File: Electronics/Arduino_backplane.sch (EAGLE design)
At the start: 40 parts, among them IC1 4013N, IC2 MCP4802, IC3 MCP4802, Q1 BF199, Q5 BF199, X1 M25-HD-20, X2 M25-HD-20

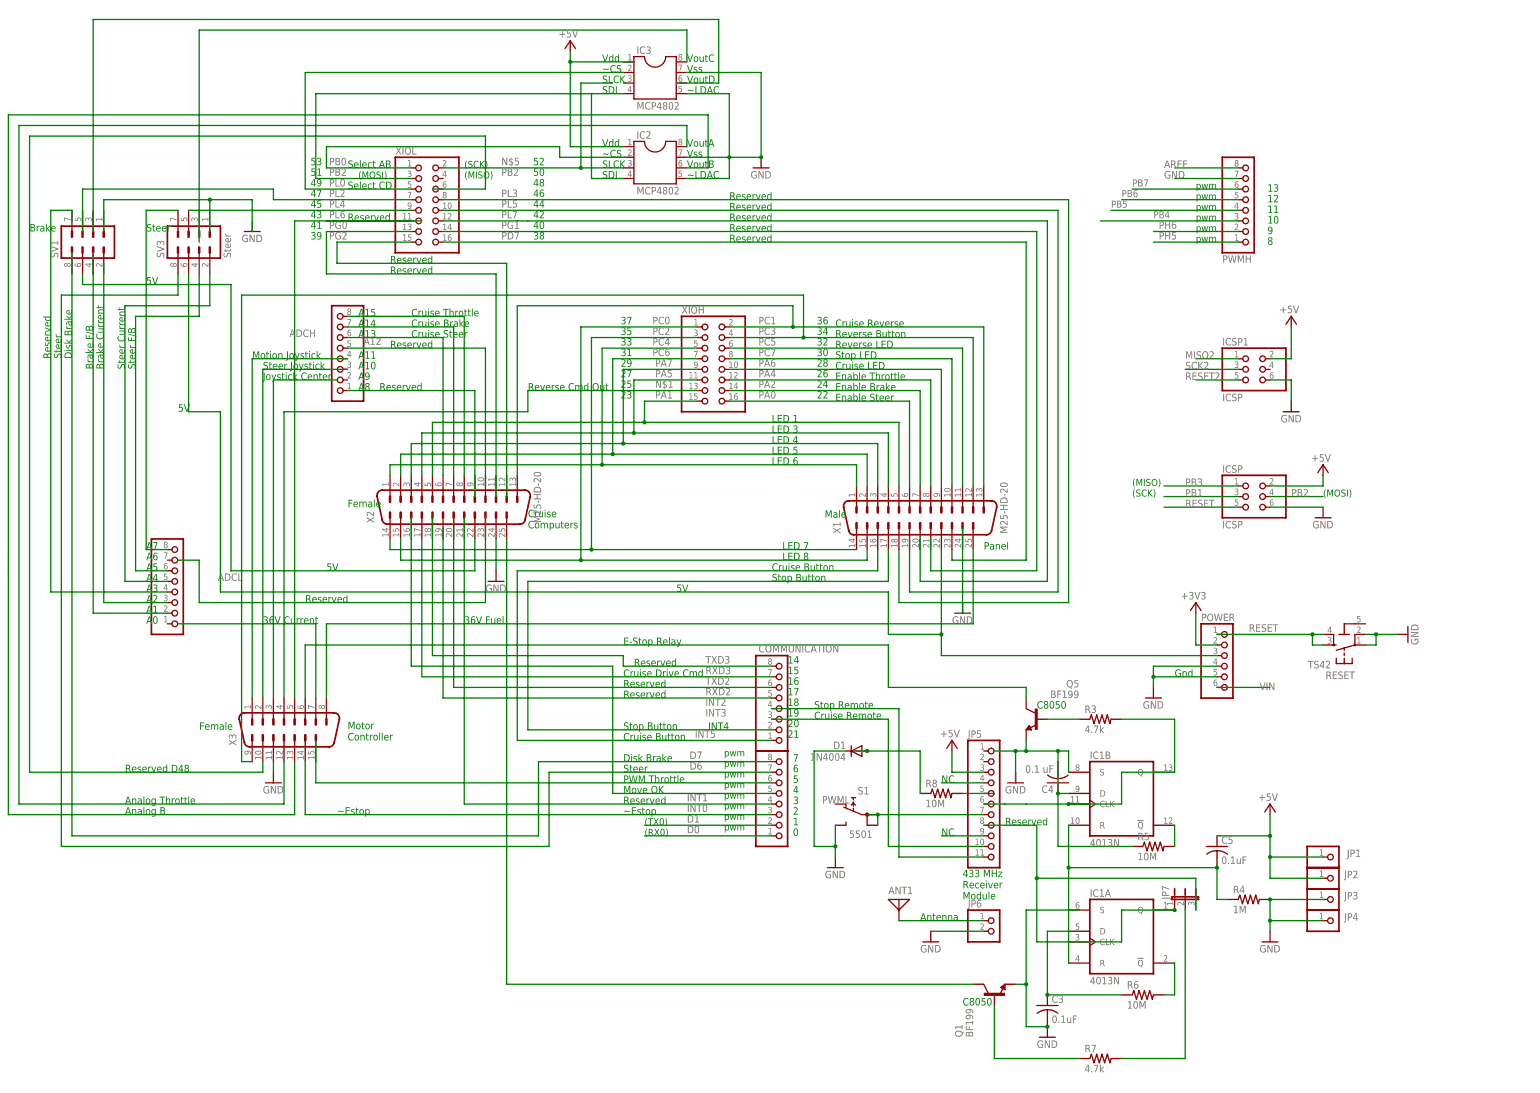
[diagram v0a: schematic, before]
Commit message: Board layout improved, closer to Arduino pins. Signals renamed.
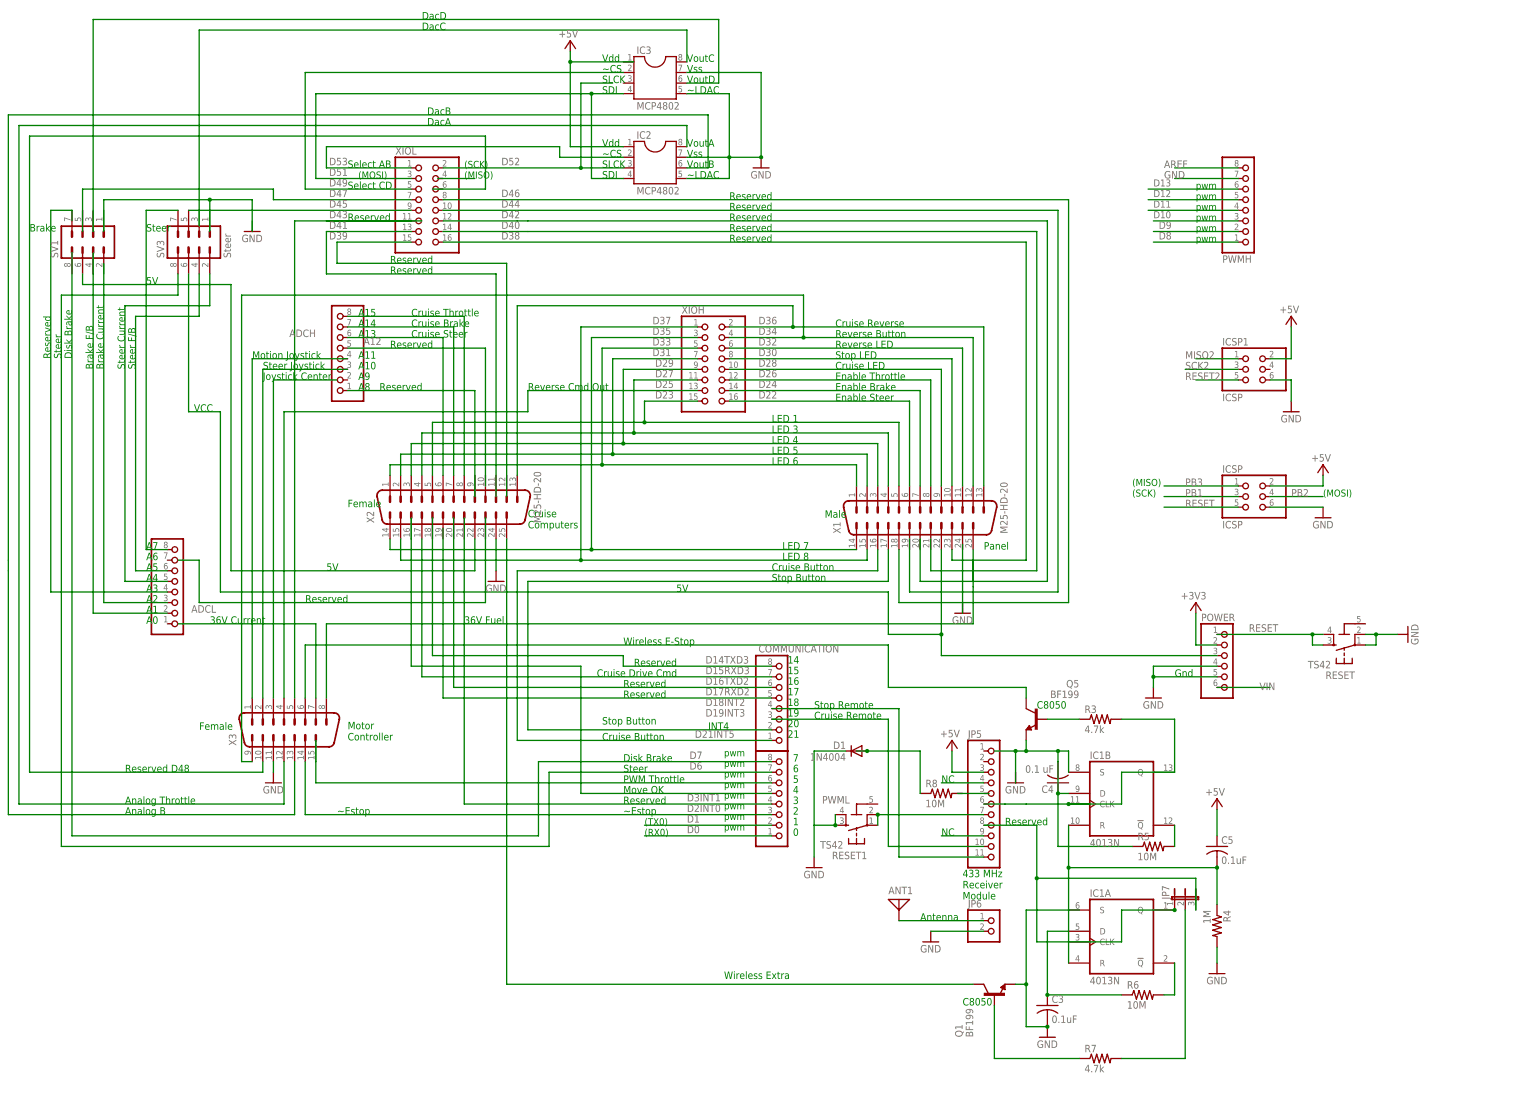
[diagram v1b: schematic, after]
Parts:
- removed JP1, JP2, JP3, JP4: (no value), pinhead:PINHD-1X1
- removed S1: 5501, switch:5501
- added RESET1: TS42, st-mod v1.4:TS42
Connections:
- net INT0 renamed D2INT0
- net INT1 renamed D3INT1
- net INT2 renamed D18INT2
- net INT3 renamed D19INT3
- net INT4 renamed D20INT4
- net INT5 renamed D21INT5
- net N$1 renamed D25
- net N$10 renamed DACC
- net N$12 renamed D48
- net N$15 renamed WLES
- net N$19 renamed FUEL
- net N$2 renamed D4
- net N$20 renamed WLX
- net N$23 renamed VCC
- net N$3 renamed DACA
- net N$4 renamed D5
- net N$5 renamed D52
- net N$6 renamed DACB
- net N$8 renamed 5V
- net N$9 renamed A7
- net PA0 renamed D22
- net PA1 renamed D23
- net PA2 renamed D24
- net PA4 renamed D26
- net PA5 renamed D27
- net PA6 renamed D28
- net PA7 renamed D29
- net PB0 renamed D53
- net PB4 renamed D10
- net PB5 renamed D11
- net PB6 renamed D12
- net PB7 renamed D13
- net PC0 renamed D37
- net PC1 renamed D36
- net PC2 renamed D35
- net PC3 renamed D34
- net PC4 renamed D33
- net PC5 renamed D32
- net PC6 renamed D31
- net PC7 renamed D30
- net PD7 renamed D38
- net PG0 renamed D41
- net PG1 renamed D40
- net PG2 renamed D39
- net PH5 renamed D8
- net PH6 renamed D9
- net PL0 renamed D49
- net PL2 renamed D47
- net PL3 renamed D46
- net PL4 renamed D45
- net PL5 renamed D44
- net PL7 renamed D42
- net RXD2 renamed D17RXD2
- net RXD3 renamed D15RXD3
- net TXD2 renamed D16TXD2
- net TXD3 renamed D14TXD3
- removed net N$13: X3.5
- removed net N$37: R8.2
- removed net PL6: XIOL.11
- new net D43: X3.5, XIOL.11
- new net D51: IC2.4, IC3.4, XIOL.3
- new net DACD: IC3.6
- net +5V: no longer JP1.1, JP2.1
- net GND: now also RESET1.3, RESET1.4; no longer JP3.1, JP4.1, S1.NO
- net N$28: now also RESET1.1, RESET1.2; no longer S1.1A, S1.1B
- net PB2: no longer IC2.4, IC3.4, XIOL.3
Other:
- note added: "DacA"
- note added: "DacB"
- note added: "DacC"
- note added: "DacD"
- note added: "VCC"
- note added: "Wireless E-Stop"
- note added: "Wireless Extra"
- note removed: "10"
- note removed: "11"
- note removed: "12"
- note removed: "13"
- note removed: "22"
- note removed: "23"
- note removed: "24"
- note removed: "25"
- note removed: "26"
- note removed: "27"
- note removed: "28"
- note removed: "29"
- note removed: "30"
- note removed: "31"
- note removed: "32"
- note removed: "33"
- note removed: "34"
- note removed: "35"
- note removed: "36"
- note removed: "37"
- note removed: "38"
- note removed: "39"
- note removed: "40"
- note removed: "41"
- note removed: "42"
- note removed: "43"
- note removed: "44"
- note removed: "45"
- note removed: "46"
- note removed: "47"
- note removed: "48"
- note removed: "49"
- note removed: "50"
- note removed: "51"
- note removed: "52"
- note removed: "53"
- note removed: "8"
- note removed: "9"
- note removed: "E-Stop Relay"
- moved on the sheet: R4

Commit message: Moved components for better routing; corrected connection errors.
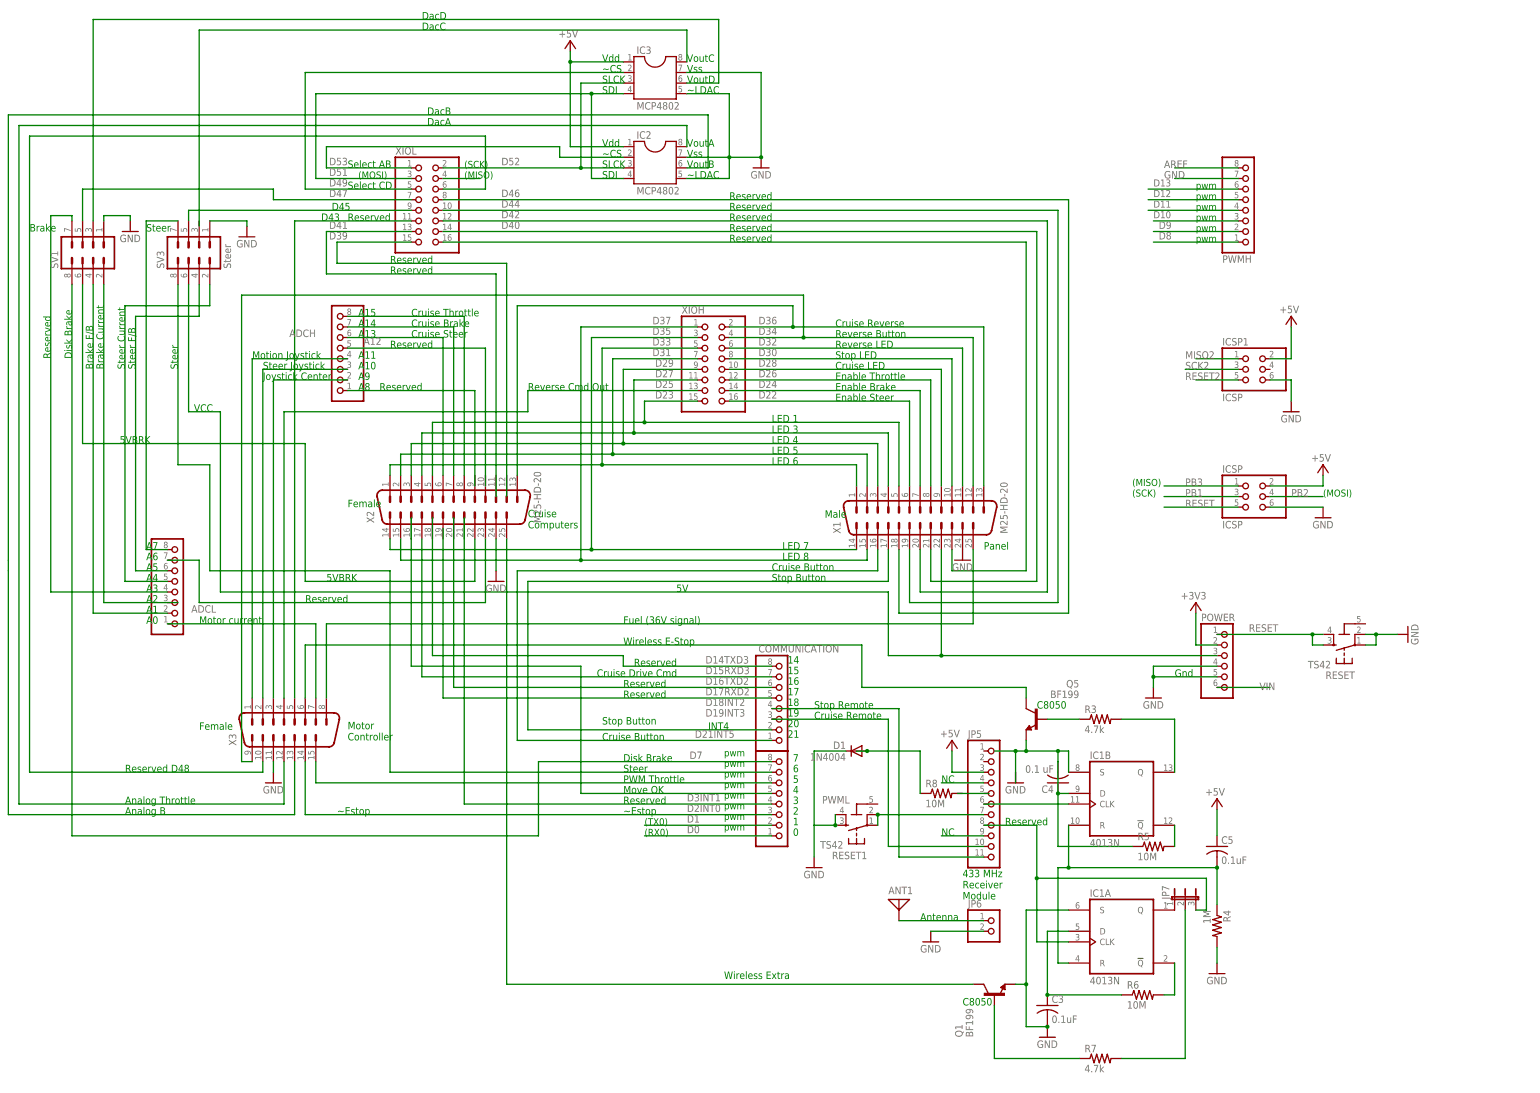
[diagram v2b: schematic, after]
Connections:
- net 5V renamed 5VBRK
- net A8 renamed N$2
- removed net A2: ADCL.3
- new net A6: ADCL.7, X2.23
- new net N$1: SV1.2
- new net N$3: XIOL.4
- new net N$4: IC1A.Q, JP7.1
- new net N$5: IC1B.Q, R3.2
- net +5V: now also IC3.1
- net A0: now also ADCL.1
- net A3: now also SV1.7
- net A9: now also ADCH.2
- net D40: now also X1.21
- net D42: now also X1.20
- net D44: now also X1.19
- net D47: now also SV1.5
- net D48: now also XIOL.6
- net D52: now also IC3.3
- net D7: now also SV1.8
- net DACD: now also SV1.3
- net GND: now also IC1A.S, SV1.1, SV3.1, X1.24
- net N$25: no longer IC1B.Q, R3.2
- net N$30: now also IC1A.CLK; no longer IC1A.Q, JP7.1
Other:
- note added: "5VBRK"
- note added: "D43"
- note added: "D45"
- note added: "Fuel (36V signal)"
- note added: "Motor current"
- note removed: "36V Current"
- note removed: "36V Fuel"
- moved on the sheet: SV1, SV3

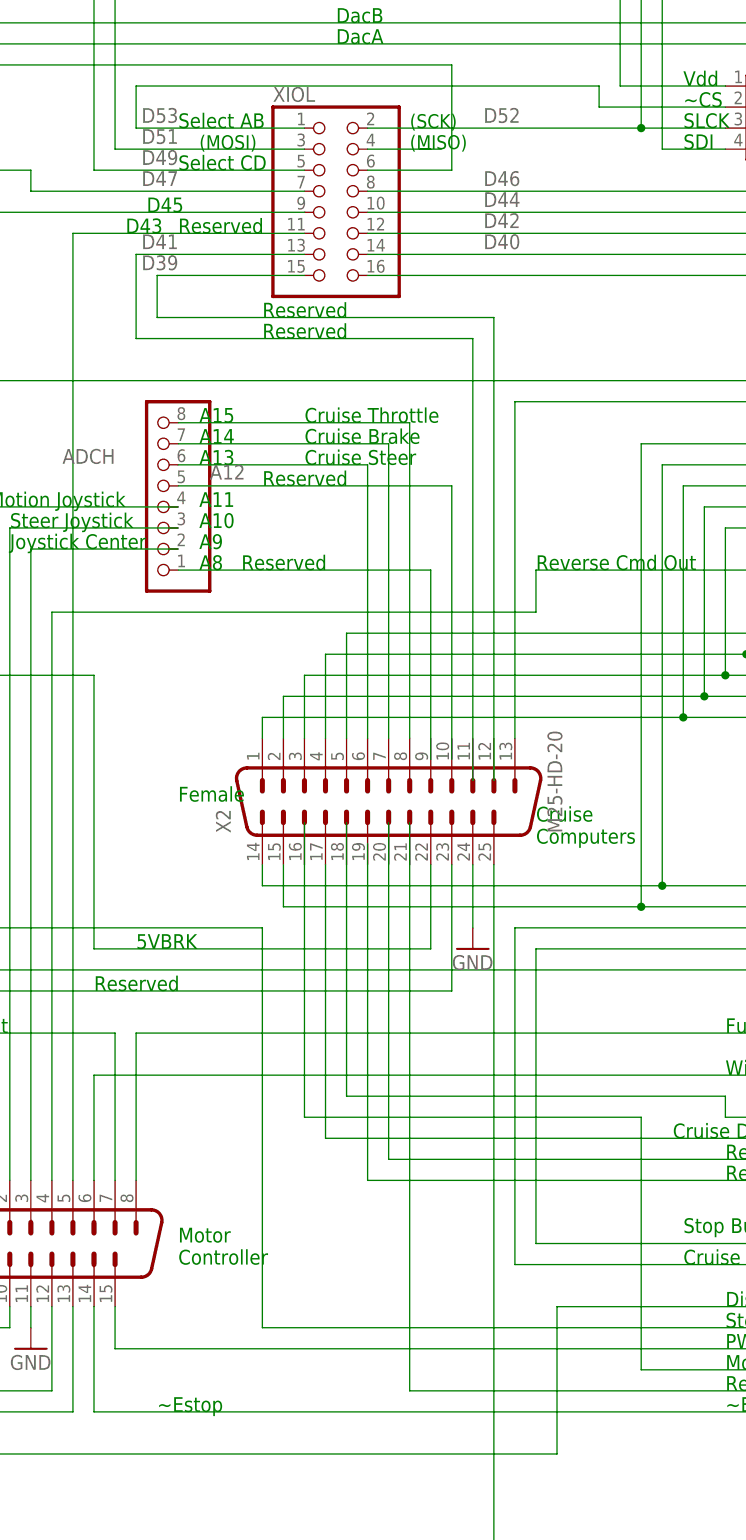
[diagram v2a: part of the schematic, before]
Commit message: Corrected some overlaps
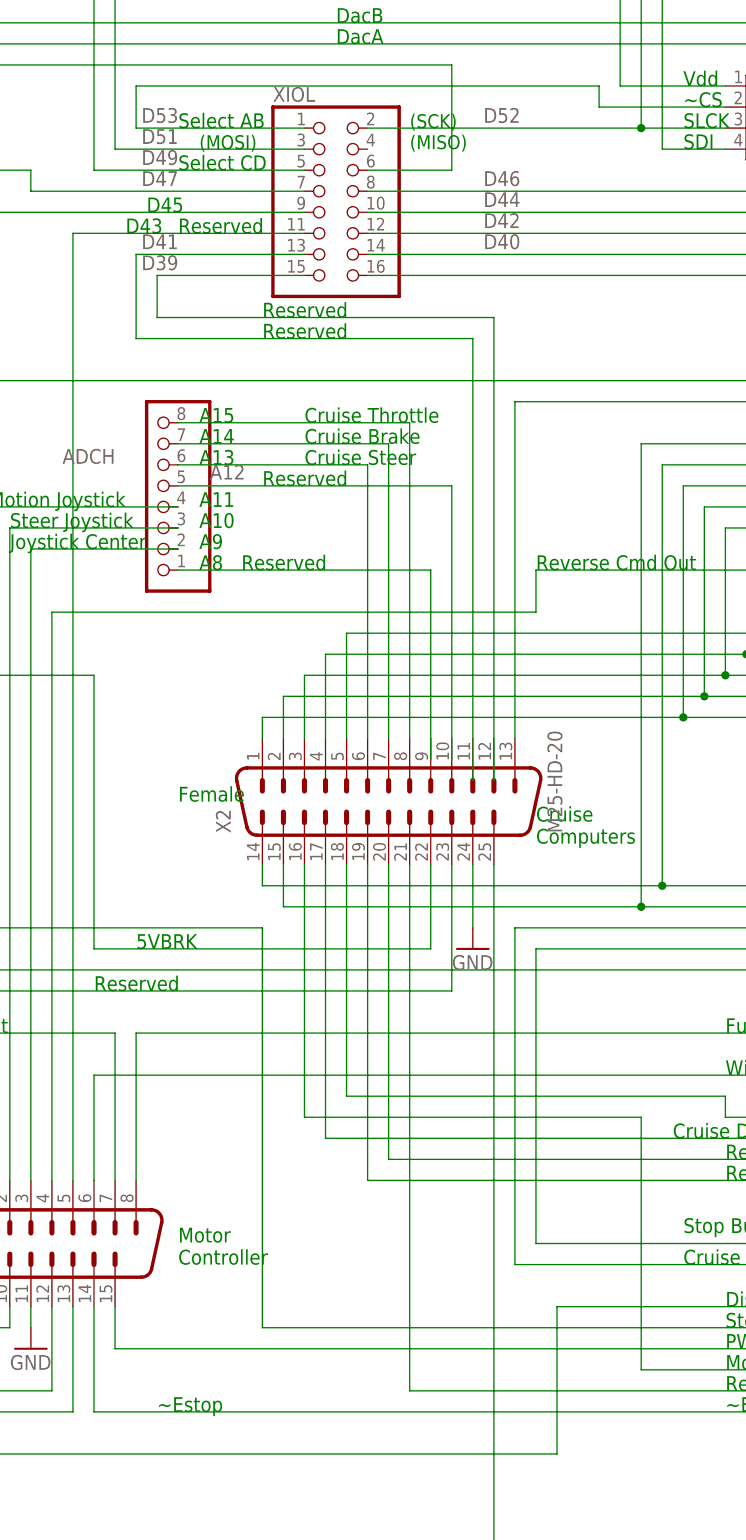
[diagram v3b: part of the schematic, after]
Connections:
- removed net N$3: XIOL.4
- net D14TXD3: now also X2.18
- net D16TXD2: now also X2.20
- net D17RXD2: now also X2.19
- net D3INT1: now also X2.21
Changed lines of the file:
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@@
 <setting verticaltext="up"/>
 </settings>
-<grid distance="0.05" unitdist="inch" unit="inch" style="lines" multiple="1" display="no" altdistance="0.01" altunitdist="inch" altunit="inch"/>
+<grid distance="0.1" unitdist="inch" unit="inch" style="lines" multiple="1" display="no" altdistance="0.01" altunitdist="inch" altunit="inch"/>
 <layers>
 <layer number="1" name="Top" color="4" fill="1" visible="no" active="no"/>
@@
 <pinref part="PWML" gate="A" pin="4"/>
 <wire x1="127" y1="35.56" x2="53.34" y2="35.56" width="0.1524" layer="91"/>
-<wire x1="53.34" y1="35.56" x2="53.34" y2="104.14" width="0.1524" layer="91"/>
+<pinref part="X2" gate="G$1" pin="21"/>
+<wire x1="53.34" y1="99.06" x2="53.34" y2="35.56" width="0.1524" layer="91"/>
 </segment>
 </net>
@@
 <pinref part="COMMUNICATION" gate="A" pin="5"/>
 <wire x1="127" y1="60.96" x2="48.26" y2="60.96" width="0.1524" layer="91"/>
-<wire x1="48.26" y1="60.96" x2="48.26" y2="101.6" width="0.1524" layer="91"/>
+<pinref part="X2" gate="G$1" pin="19"/>
+<wire x1="48.26" y1="99.06" x2="48.26" y2="60.96" width="0.1524" layer="91"/>
 </segment>
 </net>
@@
 <pinref part="COMMUNICATION" gate="A" pin="6"/>
 <wire x1="127" y1="63.5" x2="50.8" y2="63.5" width="0.1524" layer="91"/>
-<wire x1="50.8" y1="63.5" x2="50.8" y2="104.14" width="0.1524" layer="91"/>
+<pinref part="X2" gate="G$1" pin="20"/>
+<wire x1="50.8" y1="63.5" x2="50.8" y2="99.06" width="0.1524" layer="91"/>
 </segment>
 </net>
@@
 <wire x1="91.44" y1="68.58" x2="91.44" y2="71.12" width="0.1524" layer="91"/>
 <wire x1="91.44" y1="71.12" x2="45.72" y2="71.12" width="0.1524" layer="91"/>
-<wire x1="45.72" y1="71.12" x2="45.72" y2="104.14" width="0.1524" layer="91"/>
+<pinref part="X2" gate="G$1" pin="18"/>
+<wire x1="45.72" y1="99.06" x2="45.72" y2="71.12" width="0.1524" layer="91"/>
 </segment>
 </net>
@@
 <net name="D4" class="0">
 <segment>
-<wire x1="40.64" y1="99.06" x2="40.64" y2="104.14" width="0.1524" layer="91"/>
 <pinref part="X2" gate="G$1" pin="16"/>
 <wire x1="40.64" y1="99.06" x2="40.64" y2="68.58" width="0.1524" layer="91"/>
@@
 </segment>
 </net>
-<net name="D50" class="0">
-<segment>
-<wire x1="55.88" y1="185.42" x2="54.61" y2="185.42" width="0.1524" layer="91"/>
-</segment>
-</net>
 <net name="DACD" class="0">
 <segment>
@@
 </segment>
 </net>
-<net name="N$3" class="0">
-<segment>
-<pinref part="XIOL" gate="A" pin="4"/>
-<wire x1="48.26" y1="185.42" x2="57.15" y2="185.42" width="0.1524" layer="91"/>
-</segment>
-</net>
